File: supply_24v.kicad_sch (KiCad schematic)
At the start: 0 parts

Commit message: Finished motor drivers schematic
Still need to connect all the connectors and sort out old unused connections
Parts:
- added C1, C8: 330nF, Capacitor_SMD:C_0603_1608Metric, symbol Device:C
- added C10, C11, C12, C13, C2, C3, C9: 100nF, Capacitor_SMD:C_0603_1608Metric, symbol Device:C
- added C14, C5: 100pF, Capacitor_SMD:C_0603_1608Metric, symbol Device:C
- added C15, C16, C17, C18, C19, C20, C21, C22, C23, C24, C25, C26, C27, C28, C29, C30, C31, C32: 22uF, Capacitor_SMD:C_0805_2012Metric, symbol Device:C
- added C4: 4.7uF, Capacitor_SMD:C_0805_2012Metric, symbol Device:C
- added C6: 6.8nF, Capacitor_SMD:C_0603_1608Metric, symbol Device:C
- added C7: 470pF, Capacitor_SMD:C_0603_1608Metric, symbol Device:C
- added IC1: LM51231QRGRRQ1, parts:QFN50P350X350X100-21N-D, symbol parts:LM51231QRGRRQ1
- added L1: SRP1265CC-150M, parts:INDPM135125X650N, symbol parts:SRP1265CC-150M
- added Q1: ISK057N04LM6ATLA1, parts:ISK057N04LM6ATLA1, symbol parts:ISK057N04LM6ATLA1
- added Q2: ISK057N04LM6ATLA1, parts:ISK057N04LM6ATLA1, symbol SamacSys_Parts:ISK057N04LM6ATLA1
- added R1, R8: 80.6k, Resistor_SMD:R_0603_1608Metric, symbol Device:R
- added R10, R11, R12, R3, R4: 0R, Resistor_SMD:R_0603_1608Metric, symbol Device:R
- added R13: WFC08056L000FE66, parts:RESC2013X85N, symbol parts:WFC08056L000FE66
- added R14: 100R, Resistor_SMD:R_0603_1608Metric, symbol Device:R
- added R2: 100k, Resistor_SMD:R_0603_1608Metric, symbol Device:R
- added R5: 38.3k, Resistor_SMD:R_0603_1608Metric, symbol Device:R
- added R6: 21k, Resistor_SMD:R_0603_1608Metric, symbol Device:R
- added R7: 14k, Resistor_SMD:R_0603_1608Metric, symbol Device:R
- added R9: 12k, Resistor_SMD:R_0603_1608Metric, symbol Device:R
- added TP1: TestPoint_VCC, TestPoint:TestPoint_Pad_D1.0mm, symbol Connector:TestPoint
- added TP2: TestPoint_VOUT, TestPoint:TestPoint_Pad_D1.0mm, symbol Connector:TestPoint
- added TP3: TestPoint_TRK, TestPoint:TestPoint_Pad_D1.0mm, symbol Connector:TestPoint
- added TP4: TestPoint_UVLO, TestPoint:TestPoint_Pad_D1.0mm, symbol Connector:TestPoint
- added TP5: TestPoint_SW, TestPoint:TestPoint_Pad_D1.0mm, symbol Connector:TestPoint
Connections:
- new net: L1.1, R13.2, R14.2
- new net: C6.1, R5.2
- new net: C8.1, R10.2, R8.2, R9.1
- new net: IC1.15 (RT), R1.1
- new net: C1.2, IC1.17 (SS)
- new net +24V: C10.1, C2.2, C20.1, C21.1, C22.1, C23.1, C24.1, C25.1, C26.1, C27.1, C28.1, C29.1, C30.1, C31.1, C32.1, C9.1, IC1.3 (VOUT/SENSE), Q1.1 (D_1), Q1.2 (D_2), Q1.5 (D_3), Q1.6 (D_4), Q1.8 (D_5), TP2.1
- new net COMP: C5.1, IC1.20 (COMP), R5.1
- new net CSN: C14.1, IC1.2 (CSN), R14.1
- new net GND: C1.1, C10.2, C12.2, C13.2, C15.2, C16.2, C17.2, C18.2, C19.2, C2.1, C20.2, C21.2, C22.2, C23.2, C24.2, C25.2, C26.2, C27.2, C28.2, C29.2, C3.2, C30.2, C31.2, C32.2, C4.2, C5.2, C6.2, C7.2, C8.2, C9.2, IC1.10 (PGND), IC1.14 (SYNC/DITHER/VH), IC1.19 (AGND), IC1.21 (EP), Q2.4 (S_1), Q2.7 (S_2), R1.2, R4.2, R7.2, R9.2
- new net HB: C11.1, IC1.7 (HB)
- new net HO: IC1.5 (HO), Q1.3 (G)
- new net LO: IC1.11 (LO), Q2.3 (G)
- new net MCU_EN: R12.1
- new net MODE: IC1.12 (MODE), R3.1, R4.1
- new net PGOOD: IC1.4 (PGOOD), R2.1
- new net SW: C11.2, IC1.6 (SW), L1.2, Q1.4 (S_1), Q1.7 (S_2), Q2.1 (D_1), Q2.2 (D_2), Q2.5 (D_3), Q2.6 (D_4), Q2.8 (D_5), TP5.1
- new net TRK: IC1.18 (TRK), R6.2, R7.1, TP3.1
- new net UVLO: IC1.13 (UVLO/EN), R10.1, R11.1, R12.2, TP4.1
- new net VCC: C12.1, C13.1, C14.2, C15.1, C16.1, C17.1, C18.1, C19.1, C3.1, IC1.1 (CSP), IC1.8 (BIAS), R11.2, R13.1, R8.1, TP1.1
- new net VCC_DRIVER: C4.1, IC1.9 (VCC), R3.2
- new net VCC_MCU: R2.2
- new net VREF: C7.1, IC1.16 (VREF/_RANGE), R6.1
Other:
- note added: "Driver IC"
- note added: "Input Rail Capacitor Bank (110uF)"
- note added: "Light load switching mode selection FWPM - pin connected to VCC_DRIVER DEM - pin connected to GND"
- note added: "Line Undervoltage Lockout Optional: Connect to BIAS-skip V_normal: 9V V_low: 8V"
- note added: "Output Rail Capacitor Bank (286uF)"
- note added: "Output Voltage Regulation Target Vout: 24V"
- note added: "Switching loop with current sensing circuitry"
- note added: "Type-2 Loop Compensation Network Crossover frequency: 2.4kHz"
- title: (none) -> 24V Supply

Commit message: New complete schematic version
May need to resize the resistors, also need to change the caps back to electrolytic
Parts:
- removed R12: 0R, Resistor_SMD:R_0603_1608Metric, symbol Device:R
- removed TP1: TestPoint_VCC, TestPoint:TestPoint_Pad_D1.0mm, symbol Connector:TestPoint
- removed TP2: TestPoint_VOUT, TestPoint:TestPoint_Pad_D1.0mm, symbol Connector:TestPoint
- removed TP3: TestPoint_TRK, TestPoint:TestPoint_Pad_D1.0mm, symbol Connector:TestPoint
- removed TP4: TestPoint_UVLO, TestPoint:TestPoint_Pad_D1.0mm, symbol Connector:TestPoint
- removed TP5: TestPoint_SW, TestPoint:TestPoint_Pad_D1.0mm, symbol Connector:TestPoint
- added LED1: GREEN, Diode_SMD:D_0805_2012Metric, symbol Device:LED
- added Q1: DMG1012T-7, parts:SOT50P160X80-3N, symbol Device:Q_NMOS_GSD
- added R2: 100R, Resistor_SMD:R_0603_1608Metric, symbol Device:R
- added R21: 150R, Resistor_SMD:R_0603_1608Metric, symbol Device:R
- R2: value 100k -> 12k
- renumbered C15 to C36, C16 to C37, C17 to C38, C18 to C39, C19 to C40, C20 to C41, C21 to C42, C22 to C43, C23 to C44, C24 to C45, C25 to C46, C26 to C47, C27 to C48, C28 to C49, C29 to C50, C30 to C51, C31 to C52, C32 to C53
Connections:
- net GND: now also Q1.2 (S)
- net PGOOD: no longer names the net of IC1.4 (PGOOD), R2.1
- net PGOOD: now also R21.2
- net VCC_MCU renamed +5V
- net +5V: now also R2.2
- new net: LED1.2 (A), R2.1
- new net: LED1.1 (K), Q1.3 (D)
- new net: Q1.1 (G), R21.1
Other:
- moved on the sheet: C2, C5, C6, C7, C8, R10, R11, R2, R3, R4, R5, R6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

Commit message: Uploaded all project files, finished PCB design
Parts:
- removed C12: 100nF, Capacitor_SMD:C_0603_1608Metric, symbol Device:C
- removed C36, C37, C38, C39, C40, C41, C42, C43, C44, C45, C46, C47, C48, C49, C50, C51, C52, C53: 22uF, Capacitor_SMD:C_0805_2012Metric, symbol Device:C
- removed Q1: ISK057N04LM6ATLA1, parts:ISK057N04LM6ATLA1, symbol parts:ISK057N04LM6ATLA1
- removed Q2: ISK057N04LM6ATLA1, parts:ISK057N04LM6ATLA1, symbol SamacSys_Parts:ISK057N04LM6ATLA1
- removed R21: 150R, Resistor_SMD:R_0603_1608Metric, symbol Device:R
- added C13: 100nF, Capacitor_SMD:C_0603_1608Metric, symbol Device:C
- added C15, C18: 100uF, parts:CAPAE1030X1100N, symbol Device:C_Polarized
- added C16, C17: 10uF, Capacitor_SMD:C_0805_2012Metric, symbol Device:C
- added C19, C20: 10uF/50V, Capacitor_SMD:C_1206_3216Metric, symbol Device:C
- added Q2, Q3: ISZ065N03L5S, parts:ISZ065N03L5SATMA1, symbol Device:Q_NMOS_SGD
- C14, C7: footprint Capacitor_SMD:C_0603_1608Metric -> Capacitor_SMD:C_0402_1005Metric
- C5: value 100pF -> 22pF; footprint Capacitor_SMD:C_0603_1608Metric -> Capacitor_SMD:C_0402_1005Metric
- C6: value 6.8nF -> 1.5nF; footprint Capacitor_SMD:C_0603_1608Metric -> Capacitor_SMD:C_0402_1005Metric
- L1: value SRP1265CC-150M -> SRP6060FA-4R7M; footprint parts:INDPM135125X650N -> parts:SRP6060FA4R7M; symbol parts:SRP1265CC-150M -> Device:L; Manufacturer_Part_Number SRP1265CC-150M -> SRP6060FA-4R7M
- LED1: footprint Diode_SMD:D_0805_2012Metric -> LED_SMD:LED_0805_2012Metric
- R1: value 80.6k -> 32.4k/.1%
- R13: value WFC08056L000FE66 -> 0.006R; footprint parts:RESC2013X85N -> Resistor_SMD:R_0805_2012Metric; symbol parts:WFC08056L000FE66 -> Device:R
- R2: value 100R -> 150R
- R5: value 38.3k -> 59k
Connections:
- net +24V: now also C18.1, C19.1, C20.1, Q2.3 (D)
- net +5V: now also R2.1; no longer R2.2
- net GND: now also C13.2, C15.2, C16.2, C17.2, C18.2, C19.2, C20.2, Q3.1 (S)
- net HO: now also Q2.2 (G)
- net LO: now also Q3.2 (G)
- net SW: now also Q2.1 (S), Q3.3 (D)
- net VCC: now also C13.1, C15.1, C16.1, C17.1
- net at IC1.4 (PGOOD), R2.1: now also Q1.1 (G)
- net at LED1.2 (A): now also R2.2; no longer R2.1
- net VCC_DRIVER renamed VCC_REG
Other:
- note added: "4.7uH"
- note added: "Input Capacitor(s)"
- note added: "Light load switching mode selection FWPM - pin connected to VCC_REG DEM - pin connected to GND"
- note added: "Output Capacitor(s)"
- note added: "Type-2 Loop Compensation Network Crossover frequency: 8.2kHz"
- note removed: "Input Rail Capacitor Bank (110uF)"
- note removed: "Light load switching mode selection FWPM - pin connected to VCC_DRIVER DEM - pin connected to GND"
- note removed: "Output Rail Capacitor Bank (286uF)"
- note removed: "Type-2 Loop Compensation Network Crossover frequency: 2.4kHz"
- moved on the sheet: C1, C10, C11, C13, C14, C2, C3, C4, C5, C6, C9, IC1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

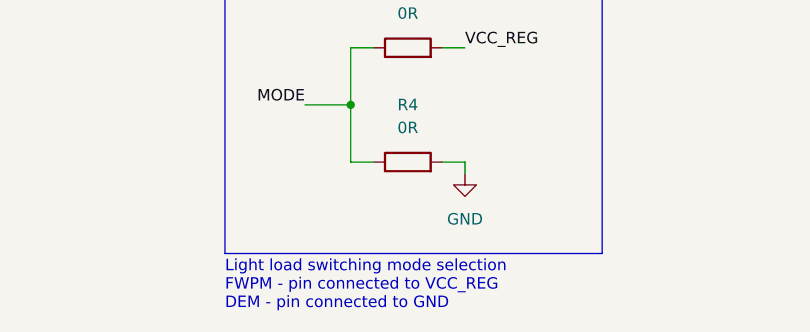
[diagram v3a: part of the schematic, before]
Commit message: Trace routing corrections, prepared for further modifications
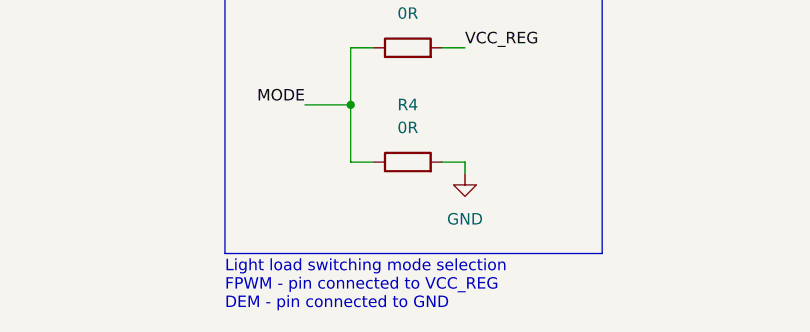
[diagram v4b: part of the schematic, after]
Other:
- note added: "Light load switching mode selection FPWM - pin connected to VCC_REG DEM - pin connected to GND"
- note removed: "Light load switching mode selection FWPM - pin connected to VCC_REG DEM - pin connected to GND"
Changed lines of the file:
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@@
     (effects (font (size 1.27 1.27)) (justify left bottom))
   )
-  (text "Light load switching mode selection\nFWPM - pin connected to VCC_REG\nDEM - pin connected to GND"
+  (text "Light load switching mode selection\nFPWM - pin connected to VCC_REG\nDEM - pin connected to GND"
     (at 132.08 170.18 0)
     (effects (font (size 1.27 1.27)) (justify left bottom))
